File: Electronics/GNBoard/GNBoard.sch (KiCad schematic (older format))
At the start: 52 parts, among them K1 IR1, K10 IR4, K11 CNY_1, K12 CNY_2, K13 CNY_3, K14 CNY_4, K17 Nose, K2 IR2, K3 SERVO_1, K4 SERVO_2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

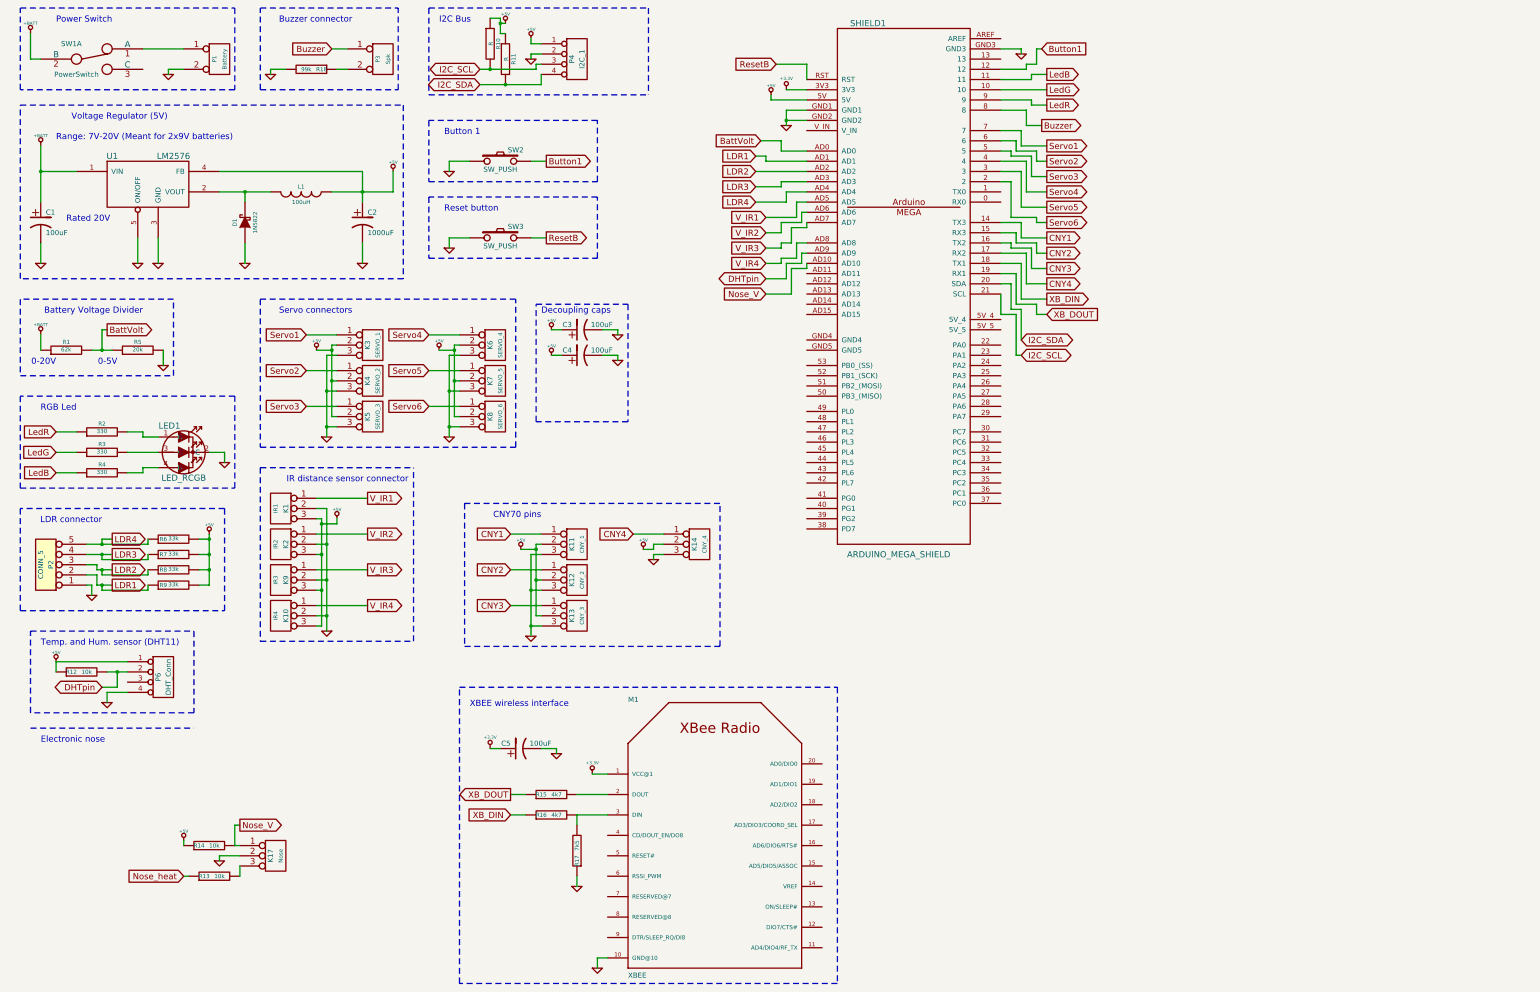
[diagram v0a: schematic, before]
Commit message: Added support for LDRs, lots of changes
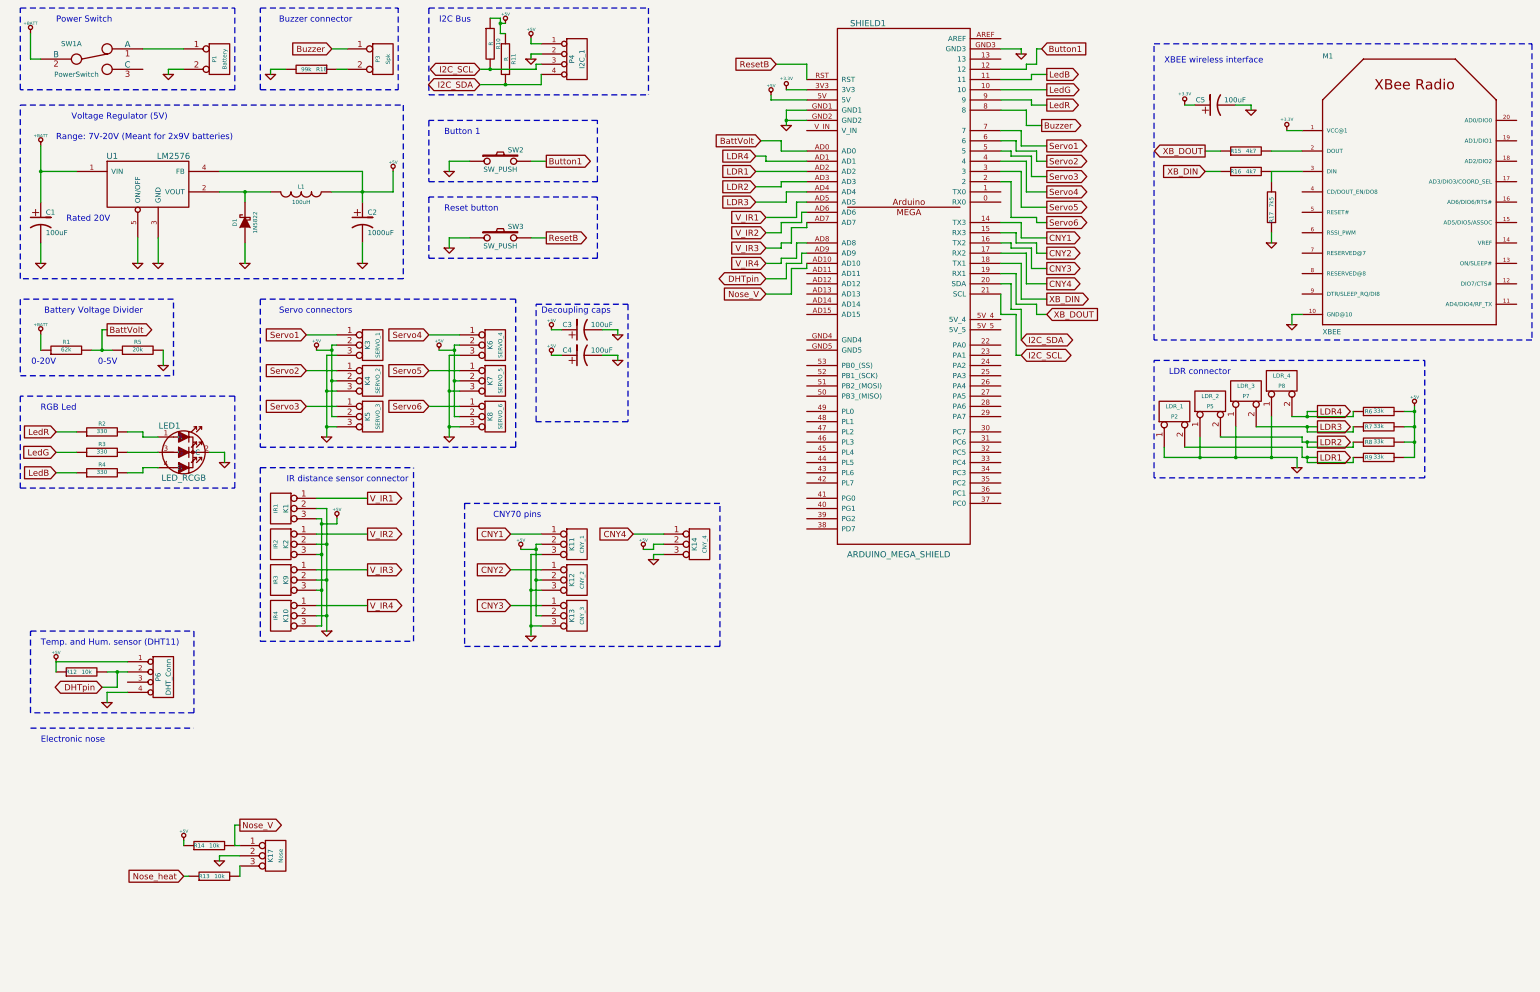
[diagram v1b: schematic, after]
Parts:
- removed P2: CONN_5, ~, symbol CONN_5
- added P2: LDR_1, ~, symbol CONN_2
- added P5: LDR_2, ~, symbol CONN_2
- added P7: LDR_3, ~, symbol CONN_2
- added P8: LDR_4, ~, symbol CONN_2
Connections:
- net GND: now also P2.1 (P1), P5.1 (P1), P7.1 (P1), P8.1 (P1)
- net LDR1: now also SHIELD1.AD2, P2.2 (PM); no longer SHIELD1.AD1
- net LDR2: now also SHIELD1.AD3, P5.2 (PM); no longer SHIELD1.AD2
- net LDR3: now also SHIELD1.AD4, P7.2 (PM); no longer SHIELD1.AD3
- net LDR4: now also SHIELD1.AD1, P8.2 (PM); no longer SHIELD1.AD4
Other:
- moved on the sheet: C5, M1, R15, R16, R17, R6, R7, R8, R9

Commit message: Finished v1.0 of the GNBoard
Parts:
- removed K17: Nose, ~, symbol CONN_3
- removed K8: SERVO_6, ~, symbol CONN_3
- added P10: Nose_Heater, ~, symbol CONN_2
- added P11: CONN_1, ~, symbol CONN_1
- added P9: Nose_Sense, ~, symbol CONN_2
- added Q1: NPN, ~, symbol NPN
- R18: value 99k -> 47
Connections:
- net Servo6 is gone; now on net Nose_heat: SHIELD1.2
- net +5V: now also P10.1 (P1), P11.1, P9.2 (PM); no longer R14.1
- net GND: now also R14.1, Q1.1 (E)
- net at R13.2: now also Q1.2 (B)
- net Nose_V renamed Nose_Vout
- net Nose_Vout: now also P9.1 (P1)
- new net: P10.2 (PM), Q1.3 (C)
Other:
- note added: "Electronic nose (TGS 2600 and alike)"
- note added: "Heater"
- note added: "Inductive loads would\nrequire flyback diode\nMinimum: 7 Ohm\n(Imax=0.8A @ 5V)"
- note added: "Sensor"
- note added: "The layout allows to solder the sensor\ndirectly or with a three wire cable"
- note removed: "Electronic nose"
- moved on the sheet: R14
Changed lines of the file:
@@
 Sheet 1 1
 Title ""
-Date "6 feb 2014"
+Date "8 feb 2014"
 Rev ""
 Comp ""
@@
 L GND #PWR021
 U 1 1 51B90FF1
-P 4800 4850
-F 0 "#PWR021" H 4800 4850 30  0001 C CNN
-F 1 "GND" H 4800 4780 30  0001 C CNN
-F 2 "" H 4800 4850 60  0000 C CNN
-F 3 "" H 4800 4850 60  0000 C CNN
-	1    4800 4850
+P 4800 4500
+F 0 "#PWR021" H 4800 4500 30  0001 C CNN
+F 1 "GND" H 4800 4430 30  0001 C CNN
+F 2 "" H 4800 4500 60  0000 C CNN
+F 3 "" H 4800 4500 60  0000 C CNN
+	1    4800 4500
 	1    0    0    -1
 $EndComp
@@
 	1    0    0    -1
 $EndComp
-$Comp
-L CONN_3 K8
-U 1 1 51B91027
-P 5250 4650
-F 0 "K8" V 5200 4650 50  0000 C CNN
-F 1 "SERVO_6" V 5300 4650 40  0000 C CNN
-F 2 "~" H 5250 4650 60  0000 C CNN
-F 3 "~" H 5250 4650 60  0000 C CNN
-	1    5250 4650
-	1    0    0    -1
-$EndComp
 Text GLabel 4600 4200 0    60   Input ~ 0
 Servo5
-Text GLabel 4600 4550 0    60   Input ~ 0
-Servo6
 $Comp
 L +5V #PWR022
@@
 Servo5
 Text GLabel 10650 2750 2    60   Output ~ 0
-Servo6
+Nose_heat
 Text GLabel 10650 2000 2    60   Output ~ 0
 Servo1
@@
 	1    0    0    -1
 $EndComp
-Text Notes 800  7850 0    60   ~ 0
-Electronic nose
-$Comp
-L R R13
-U 1 1 52F37228
-P 2500 9150
-F 0 "R13" V 2500 9250 40  0000 C CNN
-F 1 "10k" V 2500 9100 40  0000 C CNN
-F 2 "~" V 2430 9150 30  0000 C CNN
-F 3 "~" H 2500 9150 30  0000 C CNN
-	1    2500 9150
-	0    -1   -1   0
-$EndComp
+Text Notes 800  7800 0    60   ~ 0
+Electronic nose (TGS 2600 and alike)
 $Comp
 L GND #PWR042
 U 1 1 52F3722F
-P 2550 9000
-F 0 "#PWR042" H 2550 9000 30  0001 C CNN
-F 1 "GND" H 2550 8930 30  0001 C CNN
-F 2 "" H 2550 9000 60  0000 C CNN
-F 3 "" H 2550 9000 60  0000 C CNN
-	1    2550 9000
+P 2350 9800
+F 0 "#PWR042" H 2350 9800 30  0001 C CNN
+F 1 "GND" H 2350 9730 30  0001 C CNN
+F 2 "" H 2350 9800 60  0000 C CNN
+F 3 "" H 2350 9800 60  0000 C CNN
+	1    2350 9800
 	1    0    0    -1
 $EndComp
@@
 L +5V #PWR043
 U 1 1 52F37235
-P 2200 8800
-F 0 "#PWR043" H 2200 8890 20  0001 C CNN
-F 1 "+5V" H 2200 8890 30  0000 C CNN
-F 2 "" H 2200 8800 60  0000 C CNN
-F 3 "" H 2200 8800 60  0000 C CNN
-	1    2200 8800
-	1    0    0    -1
-$EndComp
-$Comp
-L CONN_3 K17
-U 1 1 52F37251
-P 3100 8950
-F 0 "K17" V 3050 8950 50  0000 C CNN
-F 1 "Nose" V 3150 8950 40  0000 C CNN
-F 2 "~" H 3100 8950 60  0000 C CNN
-F 3 "~" H 3100 8950 60  0000 C CNN
-	1    3100 8950
+P 1850 9050
+F 0 "#PWR043" H 1850 9140 20  0001 C CNN
+F 1 "+5V" H 1850 9140 30  0000 C CNN
+F 2 "" H 1850 9050 60  0000 C CNN
+F 3 "" H 1850 9050 60  0000 C CNN
+	1    1850 9050
 	1    0    0    -1
 $EndComp
@@
 	1    0    0    -1
 $EndComp
-Text GLabel 2750 8650 2    60   Output ~ 0
-Nose_V
-Text GLabel 2200 9150 0    60   Input ~ 0
+Text GLabel 2100 9450 2    60   Output ~ 0
+Nose_Vout
+Text GLabel 1300 8300 0    60   Input ~ 0
 Nose_heat
 $Comp
@@
 L R R14
 U 1 1 52F39D0D
-P 2450 8850
-F 0 "R14" V 2450 8950 40  0000 C CNN
-F 1 "10k" V 2450 8800 40  0000 C CNN
-F 2 "~" V 2380 8850 30  0000 C CNN
-F 3 "~" H 2450 8850 30  0000 C CNN
-	1    2450 8850
-	0    -1   -1   0
+P 2100 9700
+F 0 "R14" V 2100 9800 40  0000 C CNN
+F 1 "10k" V 2100 9650 40  0000 C CNN
+F 2 "~" V 2030 9700 30  0000 C CNN
+F 3 "~" H 2100 9700 30  0000 C CNN
+	1    2100 9700
+	0    1    1    0
 $EndComp
 $Comp
@@
 P 3450 1250
 F 0 "R18" V 3450 1350 40  0000 C CNN
-F 1 "99k" V 3450 1200 40  0000 C CNN
+F 1 "47" V 3450 1200 40  0000 C CNN
 F 2 "~" V 3380 1250 30  0000 C CNN
 F 3 "~" H 3450 1250 30  0000 C CNN
@@
 $EndComp
 Text GLabel 7900 3450 0    60   Input ~ 0
-Nose_V
+Nose_Vout
 Text GLabel 10650 3650 2    60   Input ~ 0
 XB_DOUT
@@
 	6250 2500 4600 2500
 Wire Wire Line
-	4800 4750 4900 4750
-Wire Wire Line
-	4800 4050 4800 4850
-Wire Wire Line
-	4800 4400 4900 4400
-Wire Wire Line
 	4800 4050 4900 4050
-Connection ~ 4800 4400
-Connection ~ 4800 4750
 Wire Wire Line
 	4900 3950 4850 3950
 Wire Wire Line
-	4850 3950 4850 4650
-Wire Wire Line
 	4850 4300 4900 4300
-Wire Wire Line
-	4850 4650 4900 4650
 Connection ~ 4850 4300
 Wire Wire Line
@@
 Wire Wire Line
 	4600 4200 4900 4200
-Wire Wire Line
-	4900 4550 4600 4550
 Wire Wire Line
 	3600 4750 3700 4750
@@
 Wire Notes Line
 	15400 3900 11700 3900
-Wire Wire Line
-	2750 8950 2550 8950
-Wire Wire Line
-	2550 8950 2550 9000
-Wire Wire Line
-	2750 8650 2700 8650
-Wire Wire Line
-	2700 8650 2700 8850
-Wire Wire Line
-	2700 8850 2750 8850
-Wire Wire Line
-	2200 8850 2200 8800
-Wire Wire Line
-	2250 9150 2200 9150
-Wire Wire Line
-	2750 9150 2750 9050
-Wire Notes Line
-	700  7700 2300 7700
 Wire Notes Line
 	4300 1450 4300 650
@@
 Wire Notes Line
 	11700 5250 11700 4100
+$Comp
+L NPN Q1
+U 1 1 52F65D79
+P 2000 8500
+F 0 "Q1" H 2000 8350 50  0000 R CNN
+F 1 "NPN" H 2000 8650 50  0000 R CNN
+F 2 "~" H 2000 8500 60  0000 C CNN
+F 3 "~" H 2000 8500 60  0000 C CNN
+	1    2000 8500
+	1    0    0    -1
+$EndComp
+Wire Wire Line
+	4850 3950 4850 4300
+Wire Wire Line
+	4800 4050 4800 4500
+Wire Wire Line
+	4900 4400 4800 4400
+Connection ~ 4800 4400
+$Comp
+L R R13
+U 1 1 52F67728
+P 1550 8400
+F 0 "R13" V 1550 8500 40  0000 C CNN
+F 1 "10k" V 1550 8350 40  0000 C CNN
+F 2 "~" V 1480 8400 30  0000 C CNN
+F 3 "~" H 1550 8400 30  0000 C CNN
+	1    1550 8400
+	0    -1   -1   0
+$EndComp
+$Comp
+L GND #PWR048
+U 1 1 52F67A77
+P 2100 8750
+F 0 "#PWR048" H 2100 8750 30  0001 C CNN
+F 1 "GND" H 2100 8680 30  0001 C CNN
+F 2 "" H 2100 8750 60  0000 C CNN
+F 3 "" H 2100 8750 60  0000 C CNN
+	1    2100 8750
+	1    0    0    -1
+$EndComp
+Wire Wire Line
+	1300 8400 1300 8300
+Wire Wire Line
+	1800 8400 1800 8500
+Wire Wire Line
+	2100 8700 2100 8750
+Wire Wire Line
+	2300 8300 2100 8300
+$Comp
+L +5V #PWR049
+U 1 1 52F6872D
+P 2250 8100
+F 0 "#PWR049" H 2250 8190 20  0001 C CNN
+F 1 "+5V" H 2250 8190 30  0000 C CNN
+F 2 "" H 2250 8100 60  0000 C CNN
+F 3 "" H 2250 8100 60  0000 C CNN
+	1    2250 8100
+	1    0    0    -1
+$EndComp
+$Comp
+L CONN_2 P10
+U 1 1 52F6858B
+P 2650 8200
+F 0 "P10" V 2600 8200 40  0000 C CNN
+F 1 "Nose_Heater" V 2700 8200 40  0000 C CNN
+F 2 "~" H 2650 8200 60  0000 C CNN
+F 3 "~" H 2650 8200 60  0000 C CNN
+	1    2650 8200
+	1    0    0    -1
+$EndComp
+Wire Wire Line
+	2300 8100 2250 8100
+Text Notes 2800 8100 0    60   ~ 0
+Inductive loads would\nrequire flyback diode\nMinimum: 7 Ohm\n(Imax=0.8A @ 5V)
+$Comp
+L CONN_2 P9
+U 1 1 52F69573
+P 1500 9450
+F 0 "P9" V 1450 9450 40  0000 C CNN
+F 1 "Nose_Sense" V 1550 9450 40  0000 C CNN
+F 2 "~" H 1500 9450 60  0000 C CNN
+F 3 "~" H 1500 9450 60  0000 C CNN
+	1    1500 9450
+	-1   0    0    1
+$EndComp
+Wire Wire Line
+	1850 9050 1850 9350
+Wire Wire Line
+	1850 9550 1850 9700
+Wire Wire Line
+	2350 9700 2350 9800
+Wire Wire Line
+	2100 9450 1950 9450
+Wire Wire Line
+	1950 9450 1950 9550
+Wire Wire Line
+	1950 9550 1850 9550
+$Comp
+L CONN_1 P11
+U 1 1 52F6A711
+P 1500 9150
+F 0 "P11" H 1580 9150 40  0000 L CNN
+F 1 "CONN_1" H 1500 9205 30  0001 C CNN
+F 2 "~" H 1500 9150 60  0000 C CNN
+F 3 "~" H 1500 9150 60  0000 C CNN
+	1    1500 9150
+	-1   0    0    1
+$EndComp
+Wire Wire Line
+	1850 9150 1650 9150
+Connection ~ 1850 9150
+Text Notes 1200 8050 0    60   ~ 0
+Heater
+Text Notes 1200 8950 0    60   ~ 0
+Sensor
+Wire Notes Line
+	700  7650 3950 7650
+Wire Notes Line
+	3950 7650 3950 9900
+Wire Notes Line
+	3950 9900 700  9900
+Wire Notes Line
+	700  9900 700  7650
+Text Notes 1950 9100 0    60   ~ 0
+The layout allows to solder the sensor\ndirectly or with a three wire cable
 $EndSCHEMATC

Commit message: Finished v1.0 of the GNBoard
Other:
- moved on the sheet: C1, C2, C3, C4, C5, D1, K1, K10, K11, K12, K13, K14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
